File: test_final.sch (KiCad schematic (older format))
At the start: 22 parts

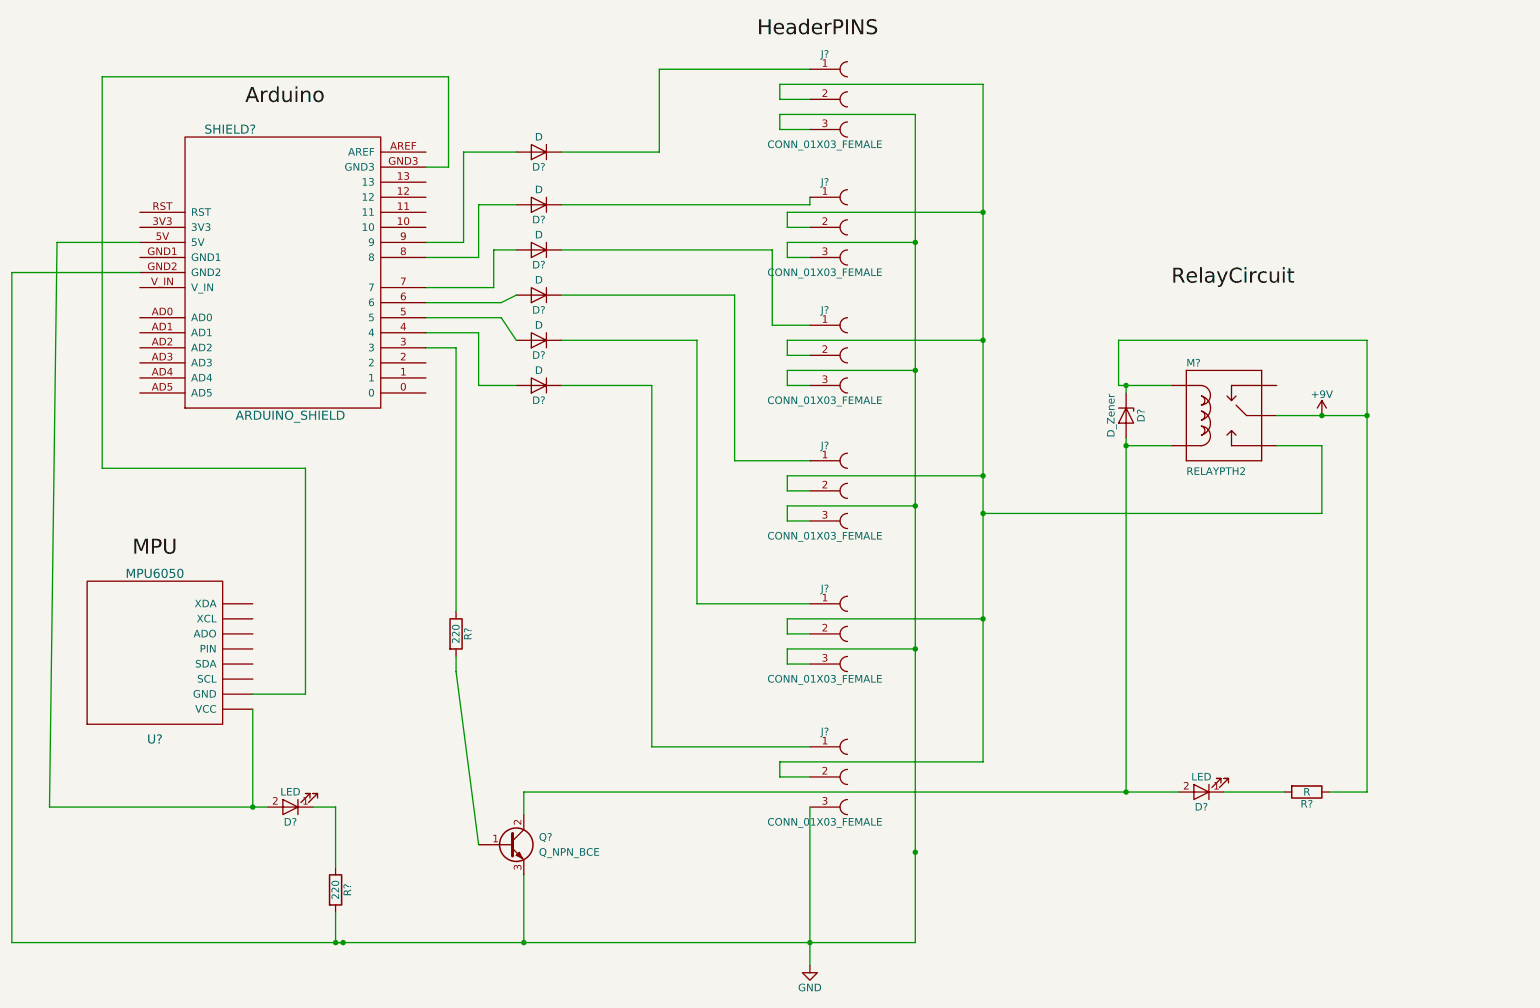
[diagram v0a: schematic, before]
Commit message: PCB with relay bugs
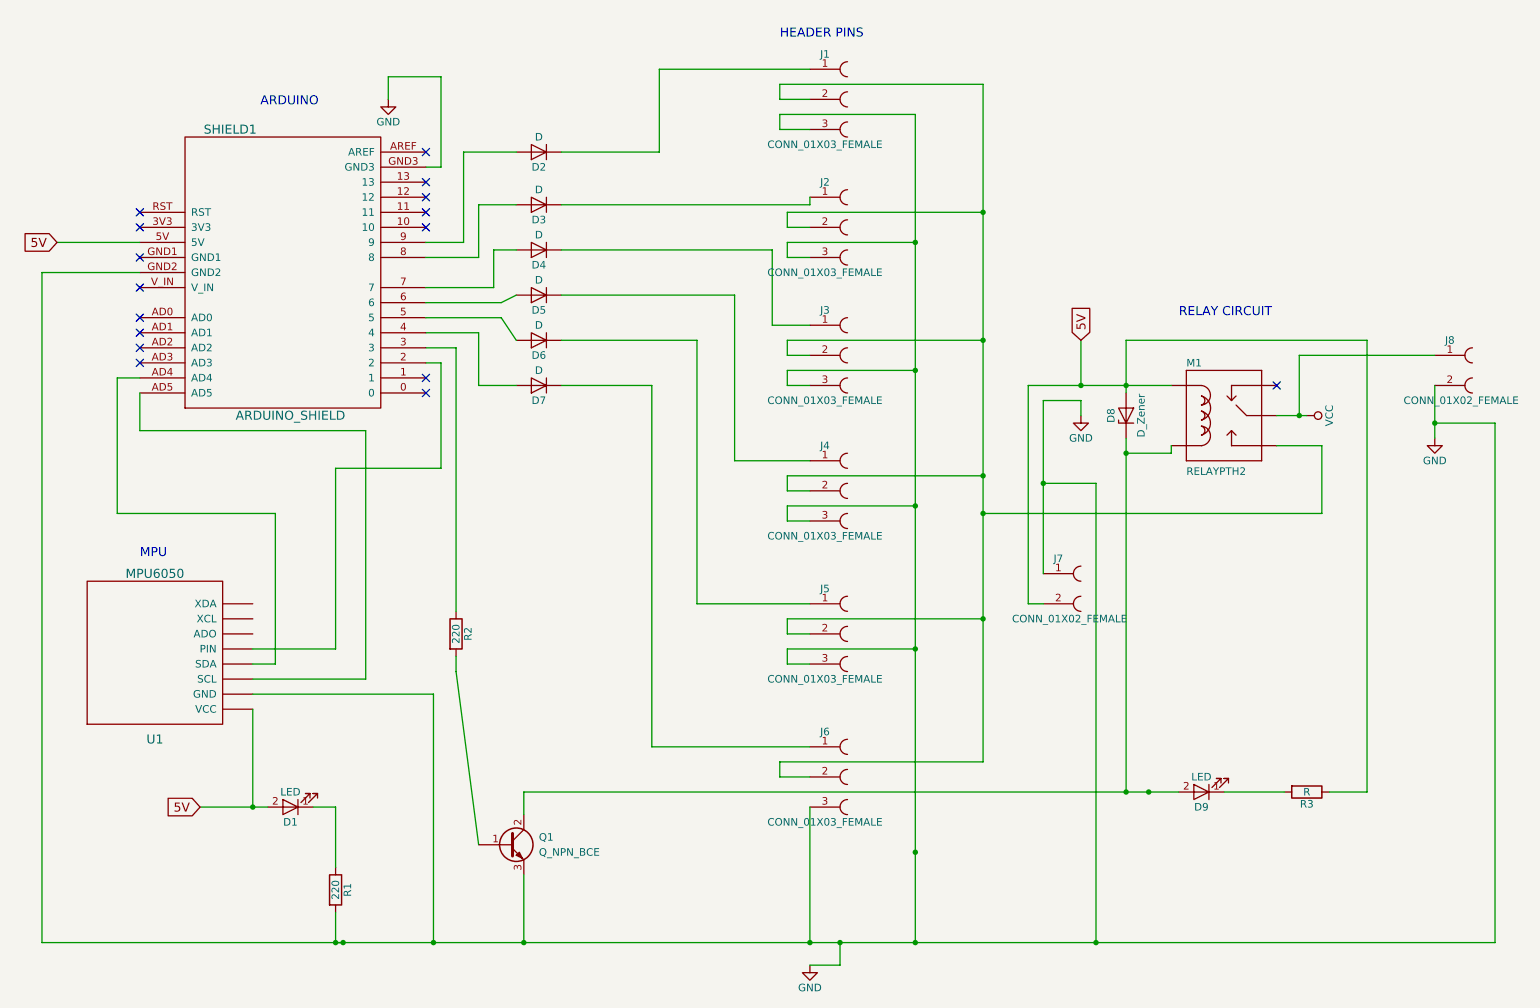
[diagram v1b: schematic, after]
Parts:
- added J7, J8: CONN_01X02_FEMALE, Pin_Headers:Pin_Header_Straight_1x03_Pitch2.54mm, symbol CONN_01X02_FEMALE
- D1, D9: renamed from D?; footprint (none) -> LEDs:LED_Rectangular_W3.0mm_H2.0mm
- D2, D3, D4, D5, D6, D7, D8: renamed from D?; footprint (none) -> Diodes_THT:D_A-405_P12.70mm_Horizontal
- J1, J2, J3, J4, J5, J6: renamed from J?; footprint (none) -> Pin_Headers:Pin_Header_Straight_1x03_Pitch2.54mm
- M1: renamed from M?; footprint RELAY-T9A -> SparkFun-Electromechanical:RELAY-T9A-2
- Q1: renamed from Q?; footprint (none) -> TO_SOT_Packages_THT:TO-126_Vertical
- R1, R2, R3: renamed from R?; footprint (none) -> Resistors_THT:R_Axial_DIN0204_L3.6mm_D1.6mm_P5.08mm_Horizontal
- SHIELD1: renamed from SHIELD?; footprint (none) -> arduino_shields:ARDUINO SHIELD
- U1: renamed from U?; footprint (none) -> Pin_Headers:Pin_Header_Straight_1x07_Pitch2.00mm
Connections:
- net at SHIELD1.2: now also U1.~ (XDA)
- net 5V: now reaches D1.2 (A), SHIELD1.5V, U1.~ (XDA)
- net 5V: now also D8.2 (A), M1.C1 (COIL1), R3.1, J7.2
- net at SHIELD1.AD4: now also U1.~ (XDA)
- net at SHIELD1.AD5: now also U1.~ (XDA)
- net at J1.3, J2.3, J3.3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: now also U1.~ (XDA), J7.1, J8.2
- net at SHIELD1.GND3: no longer U1.~ (XDA)
- net at D9.2 (A), M1.C2 (COIL2), Q1.2 (C): now also D8.1 (K); no longer D8.2 (A)
- removed net +9V: D8.1 (K), M1.C1 (COIL1), M1.MAIN, R3.1
- new net: J8.1, M1.MAIN
- no-connect marks 0 -> 16
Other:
- note added: "ARDUINO\n"
- note added: "HEADER PINS\n"
- note added: "MPU\n"
- note added: "RELAY CIRCUIT\n"
